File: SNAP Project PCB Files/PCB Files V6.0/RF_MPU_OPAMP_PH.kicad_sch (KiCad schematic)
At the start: 54 parts, among them IC2 STM32WB35CCU7A, Q4 SFH 310, SW2 SW_Push, SW3 SW_Push, SW4 SW_Push, SW5 SW_Push, U5 LT1077CN8, U6 LT1077CN8, U7 LT1077CN8, Y1 XRCGB32M000F0Z00R0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

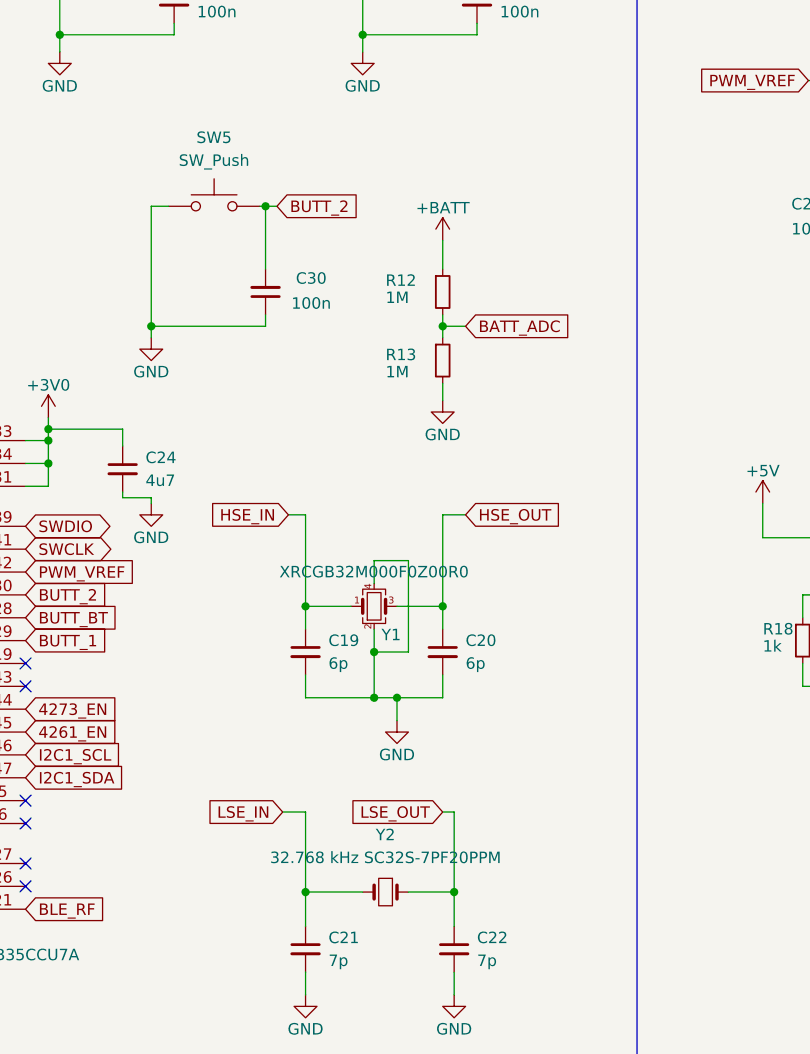
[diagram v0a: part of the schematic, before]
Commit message: OLED Screen Fix & Board corrections
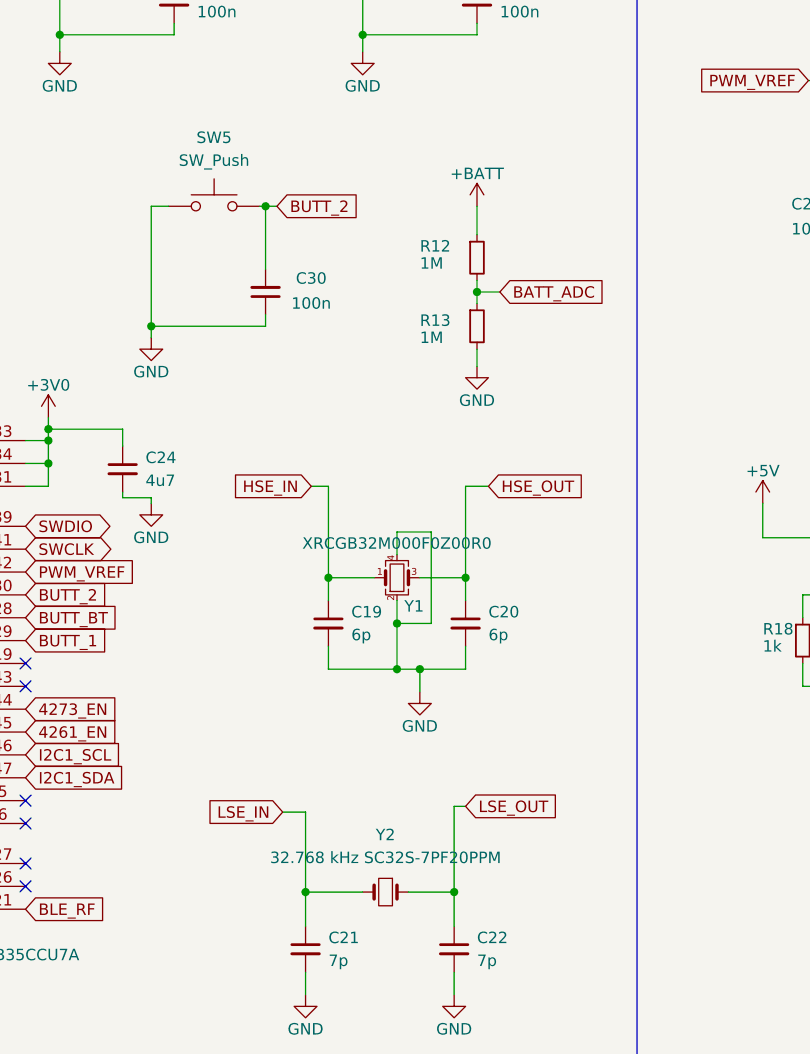
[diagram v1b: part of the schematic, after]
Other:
- moved on the sheet: C19, C20, R12, R13, Y1
